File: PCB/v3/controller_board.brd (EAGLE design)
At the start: 150 x 66 mm, 50 parts, among them M1 B4B-PH-K-S(LF)(SN), M1_TMC TMC2209_SILENTSTEPSTICK, M2 B4B-PH-K-S(LF)(SN), M2_TMC TMC2209_SILENTSTEPSTICK, M3 B4B-PH-K-S(LF)(SN), M3_TMC TMC2209_SILENTSTEPSTICK, M4 B4B-PH-K-S(LF)(SN), M4_TMC TMC2209_SILENTSTEPSTICK

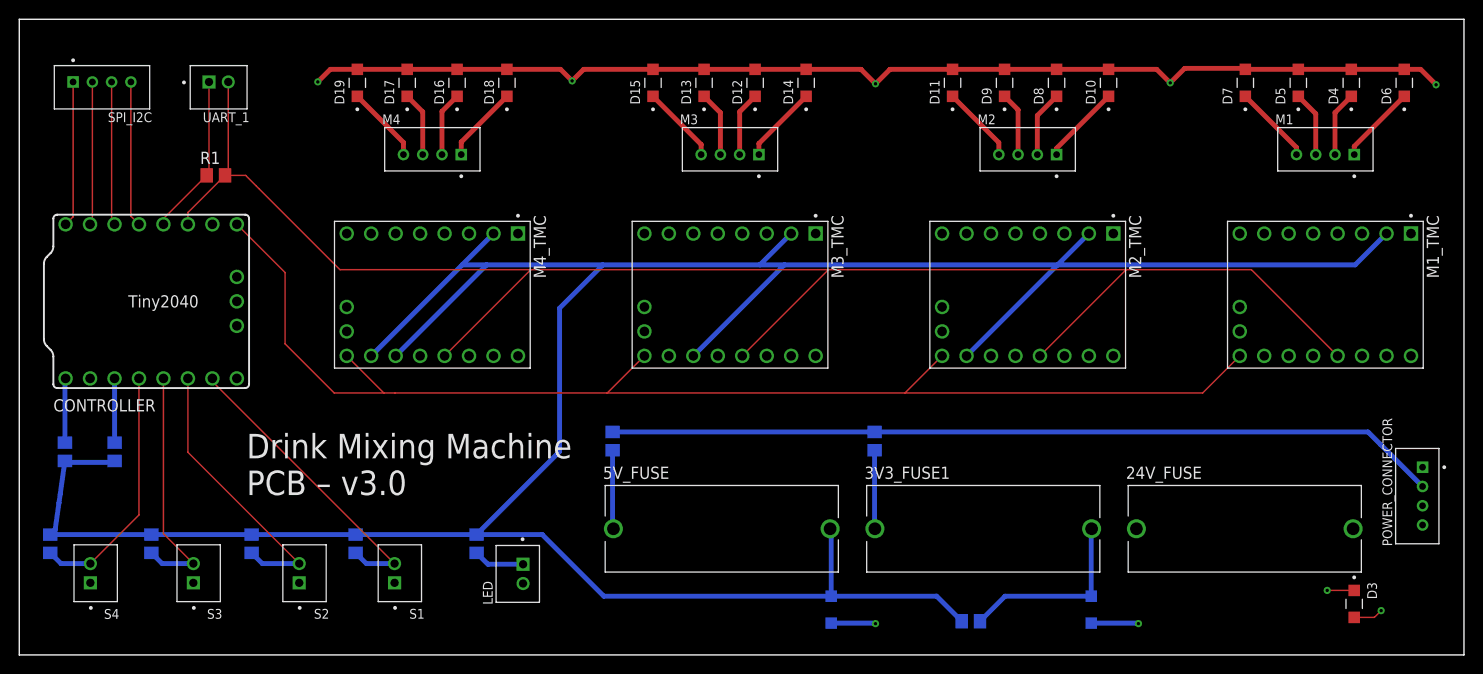
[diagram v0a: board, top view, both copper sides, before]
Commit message: fix(pcb): fix tiny2040 library
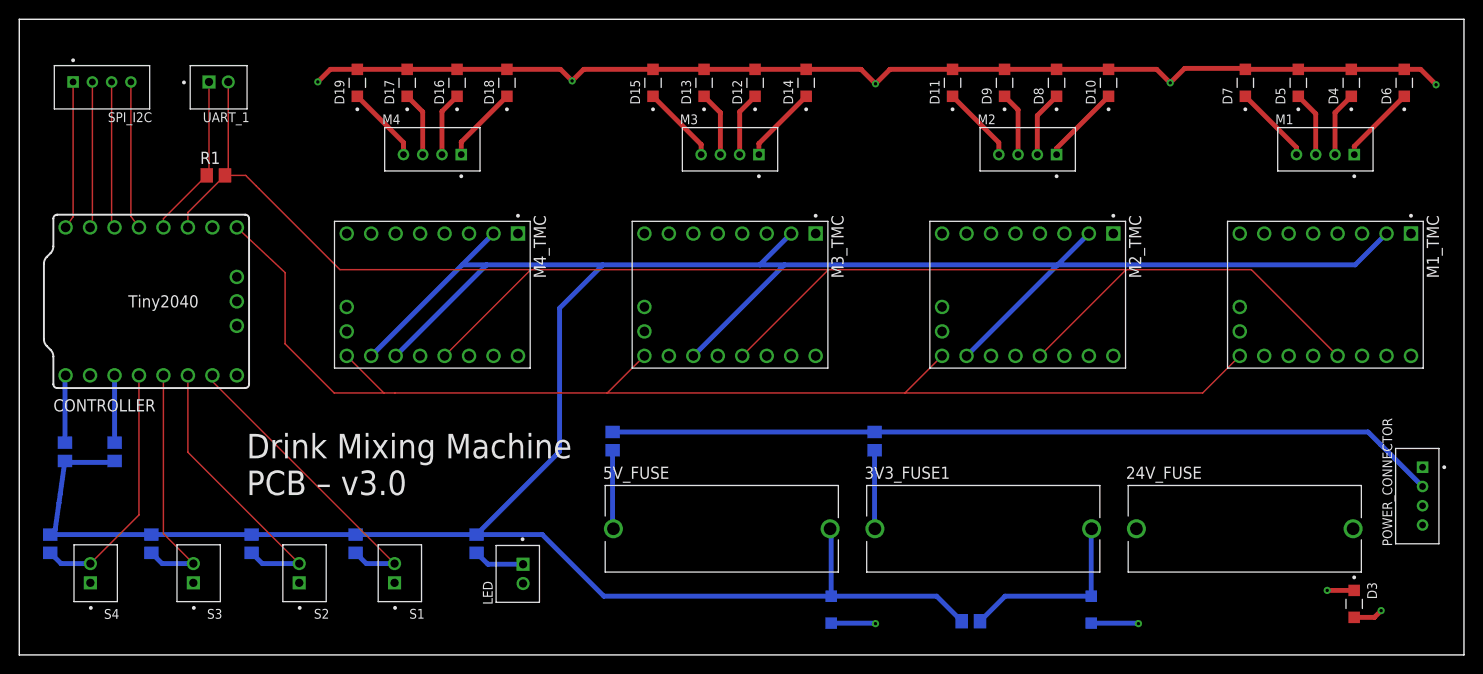
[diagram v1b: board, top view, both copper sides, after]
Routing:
- net 24V: track 188.9 -> 177.2 mm

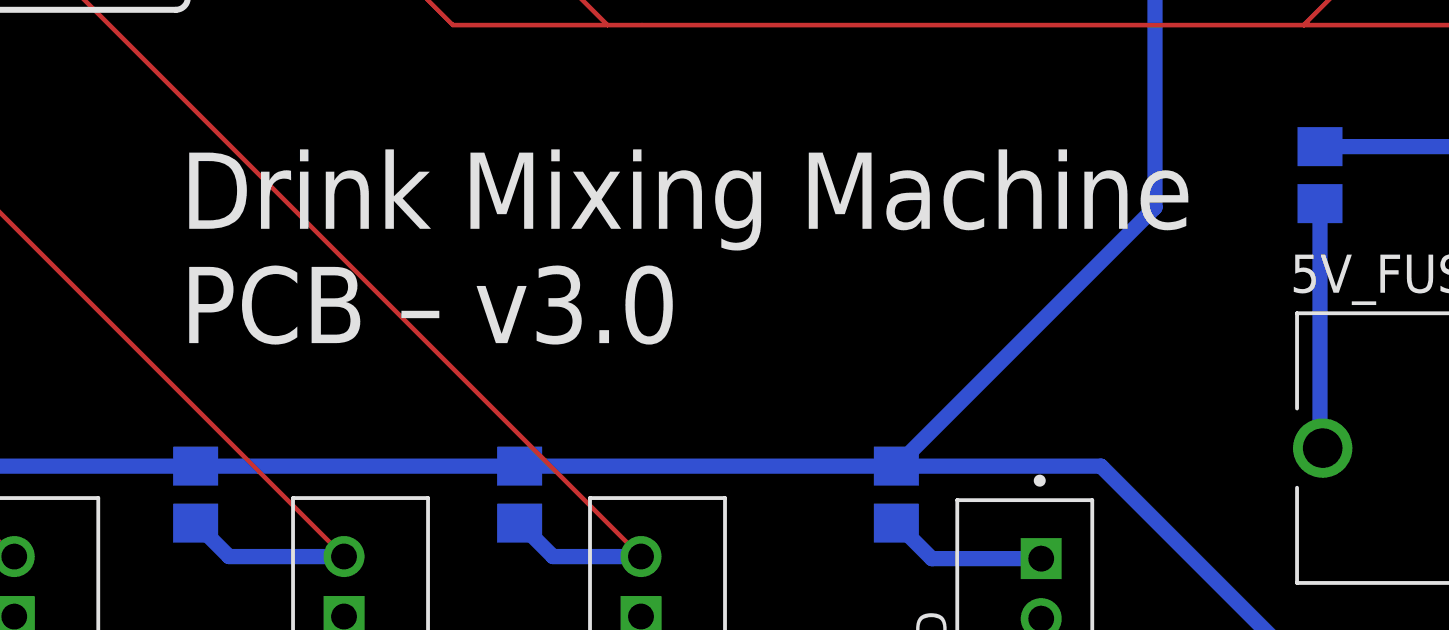
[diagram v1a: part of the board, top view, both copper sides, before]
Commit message: fix(schmatic): update UART resistor value
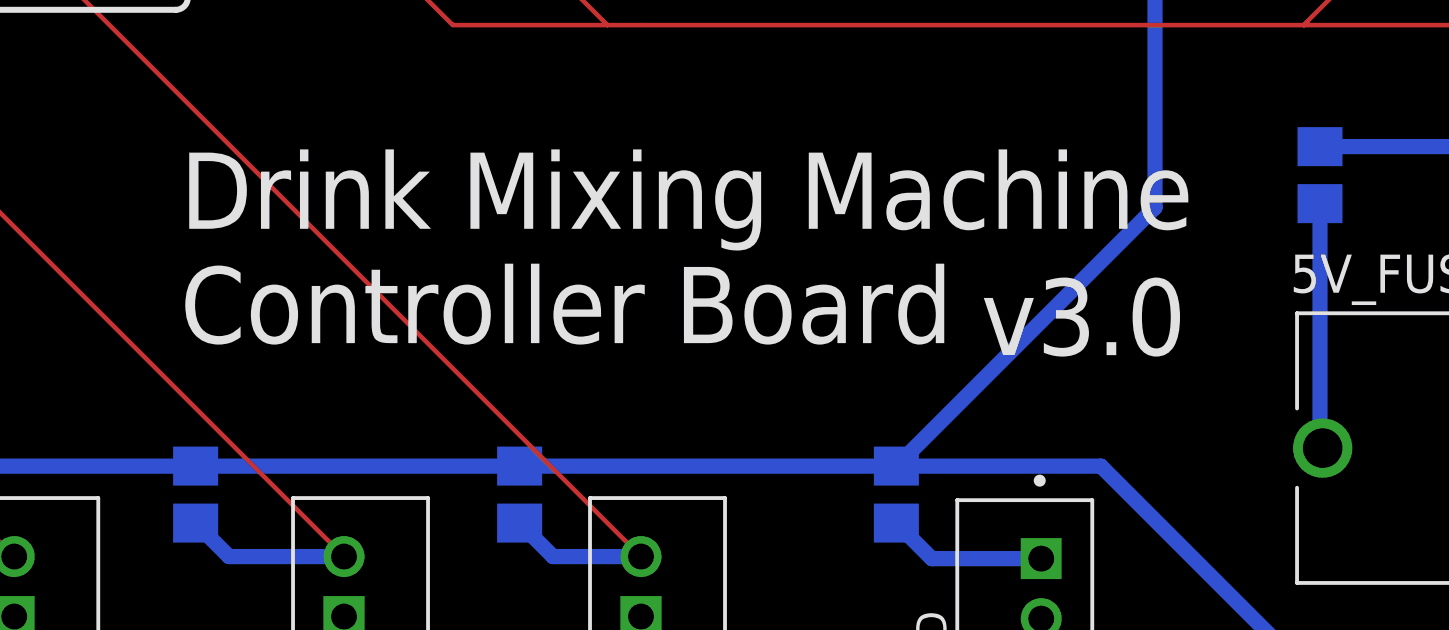
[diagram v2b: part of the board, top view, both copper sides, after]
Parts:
- R1: value 10kR -> 270R
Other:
- board text added: ">REVISION"
- board text added: "Drink Mixing Machine Controller Board"
- board text removed: "Drink Mixing Machine PCB – v3.0"
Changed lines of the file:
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@@
 <layer number="25" name="tNames" color="7" fill="1" visible="yes" active="yes"/>
 <layer number="26" name="bNames" color="7" fill="1" visible="no" active="yes"/>
-<layer number="27" name="tValues" color="7" fill="1" visible="no" active="yes"/>
+<layer number="27" name="tValues" color="7" fill="1" visible="yes" active="yes"/>
 <layer number="28" name="bValues" color="7" fill="1" visible="no" active="yes"/>
 <layer number="29" name="tStop" color="7" fill="3" visible="no" active="yes"/>
@@
 <wire x1="0" y1="66" x2="0" y2="0" width="0" layer="20"/>
 <text x="23.6" y="16.6" size="2.54" layer="25">Drink Mixing Machine
-PCB – v3.0</text>
+Controller Board</text>
+<text x="50.3" y="16.2" size="2.54" layer="25">&gt;REVISION</text>
 </plain>
 <attributes>
+<attribute name="REVISION" value="v3.0"/>
 </attributes>
 <variantdefs>
@@
 <attribute name="PRICE" value="None" x="223.89" y="71.1" size="1.778" layer="27" rot="R90" display="off"/>
 </element>
-<element name="R1" library="rcl" library_urn="urn:adsk.eagle:library:334" package="R0805" package3d_urn="urn:adsk.eagle:package:23553/2" value="10kR" x="20.4125" y="49.79" smashed="yes">
+<element name="R1" library="rcl" library_urn="urn:adsk.eagle:library:334" package="R0805" package3d_urn="urn:adsk.eagle:package:23553/2" value="270R" x="20.4125" y="49.79" smashed="yes">
 <attribute name="NAME" x="18.7775" y="50.98" size="1.27" layer="25"/>
 <attribute name="POPULARITY" value="86" x="110.5825" y="-36.57" size="1.778" layer="27" display="off"/>
